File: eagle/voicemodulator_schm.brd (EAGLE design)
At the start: 80 x 83.5 mm, 27 parts, among them T1 2N5089, T2 2N5089, T3 2N5089, T4 2N5089

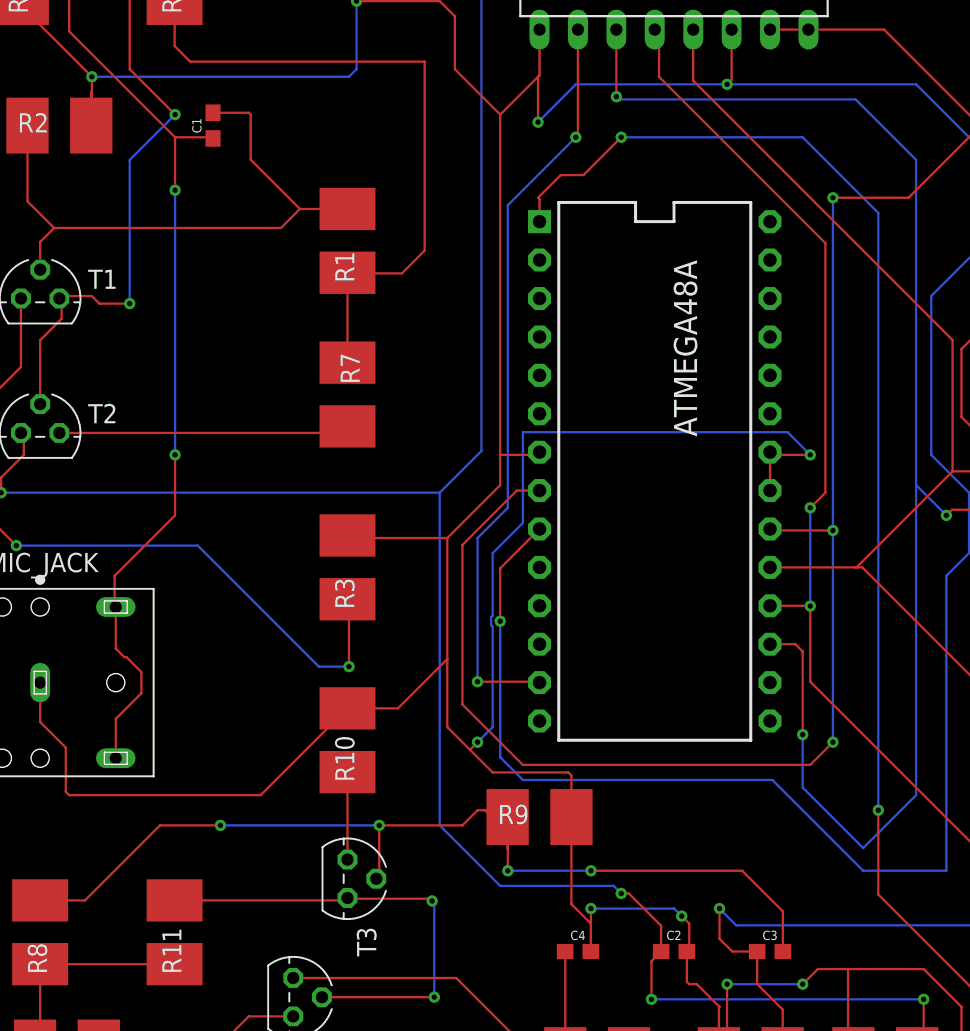
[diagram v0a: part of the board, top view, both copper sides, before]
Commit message: Pullup resistor added, testpoints at ADC in and DAC out added.
Pictures, board layout and schematic all updated.
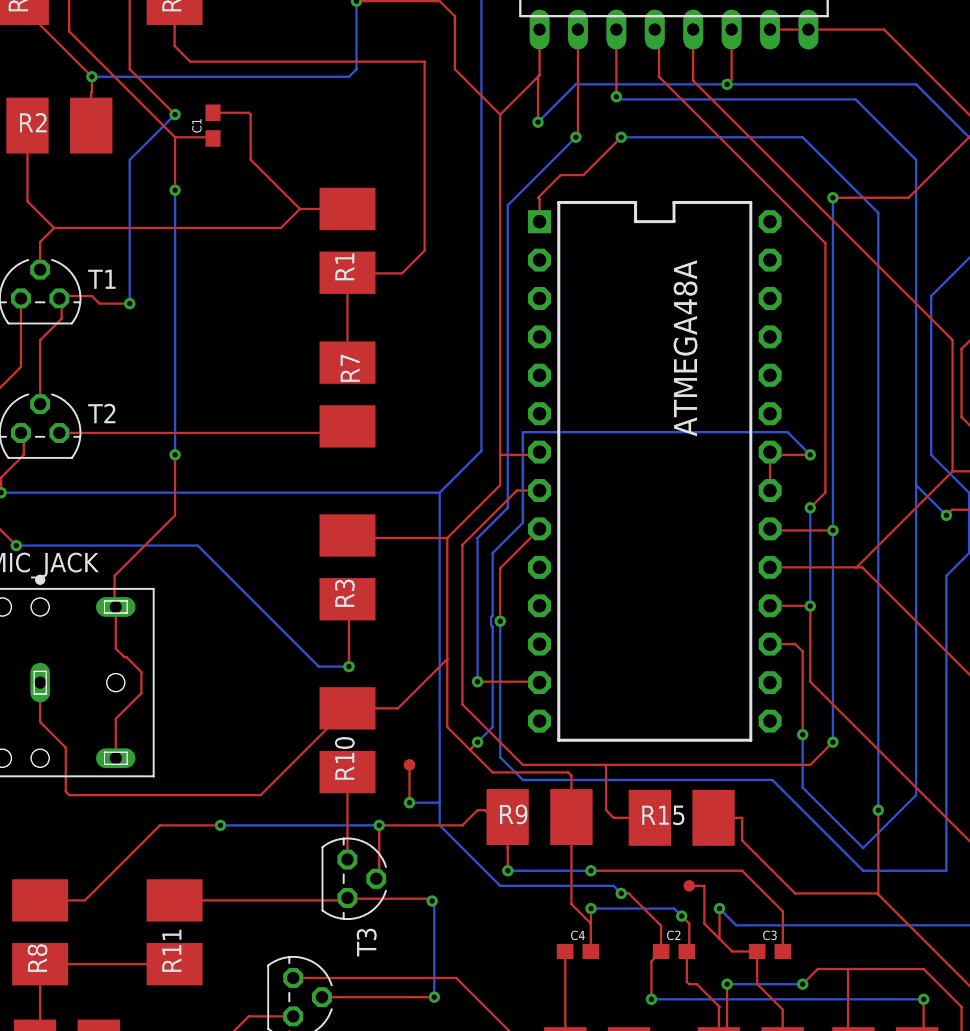
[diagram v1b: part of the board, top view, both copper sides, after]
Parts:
- added R15: (no value), resistor-shunt:SMS-WAV
- added TP1, TP2: TEST-POINT3, SparkFun-Connectors:PAD.03X.03
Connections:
- net N$22: now also R15.1
- net N$4: now also TP1.P$1
- net N$5: now also TP2.P$1
- net VCC: now also R15.2
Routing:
- net N$22: track 84.0 -> 97.9 mm
- net VCC: track 203.6 -> 209.7 mm
- net N$4: track 91.2 -> 96.2 mm
- net N$5: track 143.3 -> 147.8 mm, vias 5 -> 6
- net N$9: track 64.7 -> 62.7 mm
- net 0: track 360.4 -> 358.9 mm
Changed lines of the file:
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@@
 <attribute name="VALUE" x="20.54" y="3.965" size="1.27" layer="27" ratio="10" rot="R270"/>
+</element>
+<element name="TP1" library="SparkFun-Connectors" library_urn="urn:adsk.eagle:library:513" package="PAD.03X.03" package3d_urn="urn:adsk.eagle:package:38286/1" value="TEST-POINT3" x="48" y="14.5"/>
+<element name="TP2" library="SparkFun-Connectors" library_urn="urn:adsk.eagle:library:513" package="PAD.03X.03" package3d_urn="urn:adsk.eagle:package:38286/1" value="TEST-POINT3" x="29.5" y="22.5"/>
+<element name="R15" library="resistor-shunt" library_urn="urn:adsk.eagle:library:346" package="SMS-WAV" package3d_urn="urn:adsk.eagle:package:25223/1" value="" x="47.5" y="19">
+<attribute name="MF" value="" x="47.5" y="19" size="1.778" layer="27" display="off"/>
+<attribute name="MPN" value="" x="47.5" y="19" size="1.778" layer="27" display="off"/>
+<attribute name="NAME" x="44.7314" y="18.5428" size="1.27" layer="25"/>
+<attribute name="OC_FARNELL" value="unknown" x="47.5" y="19" size="1.778" layer="27" display="off"/>
+<attribute name="OC_NEWARK" value="unknown" x="47.5" y="19" size="1.778" layer="27" display="off"/>
+<attribute name="VALUE" x="44.452" y="16.1044" size="1.27" layer="27"/>
 </element>
 </elements>
@@
 <via x="8.5" y="68" extent="1-16" drill="0.35"/>
 <wire x1="8.5" y1="68" x2="8.5" y2="67" width="0.1524" layer="1"/>
-<wire x1="8.5" y1="67" x2="8.5" y2="65.5" width="0.1524" layer="1"/>
 <wire x1="8.5" y1="68" x2="3.81" y2="72.69" width="0.1524" layer="1"/>
 <wire x1="3.81" y1="72.69" x2="3.81" y2="72.8218" width="0.1524" layer="1"/>
@@
 <wire x1="31.5" y1="40.5" x2="2.5" y2="40.5" width="0.1524" layer="16"/>
 <via x="2.5" y="40.5" extent="1-16" drill="0.35"/>
-<wire x1="31.5" y1="40.5" x2="31.5" y2="18.5" width="0.1524" layer="16"/>
+<wire x1="31.5" y1="40.5" x2="31.5" y2="20" width="0.1524" layer="16"/>
+<wire x1="31.5" y1="20" x2="31.5" y2="18.5" width="0.1524" layer="16"/>
 <wire x1="31.5" y1="18.5" x2="35.5" y2="14.5" width="0.1524" layer="16"/>
 <wire x1="35.5" y1="14.5" x2="43" y2="14.5" width="0.1524" layer="16"/>
@@
 <wire x1="63.5" y1="7" x2="63.5" y2="3.7418" width="0.1524" layer="1"/>
 <wire x1="63.5" y1="3.7418" x2="63.0682" y2="3.31" width="0.1524" layer="1"/>
+<contactref element="TP2" pad="P$1"/>
+<wire x1="31.5" y1="20" x2="29.5" y2="20" width="0.1524" layer="16"/>
+<via x="29.5" y="20" extent="1-16" drill="0.35"/>
+<wire x1="29.5" y1="20" x2="29.5" y2="22.5" width="0.1524" layer="1"/>
 </signal>
 <signal name="N$6">
@@
 <wire x1="76" y1="51.5" x2="76.2" y2="51.3" width="0.1524" layer="1"/>
 <wire x1="76.2" y1="51.3" x2="76.2" y2="46.99" width="0.1524" layer="1"/>
+<contactref element="TP1" pad="P$1"/>
+<wire x1="50" y1="11" x2="49" y2="12" width="0.1524" layer="1"/>
+<wire x1="49" y1="12" x2="49" y2="14.5" width="0.1524" layer="1"/>
+<wire x1="49" y1="14.5" x2="48" y2="14.5" width="0.1524" layer="1"/>
 </signal>
 <signal name="N$9">
@@
 <wire x1="33" y1="18.5" x2="34" y2="19.5" width="0.1524" layer="1"/>
 <wire x1="34" y1="19.5" x2="34.5" y2="19.5" width="0.1524" layer="1"/>
-<wire x1="34.5" y1="19.5" x2="35.5418" y2="19.5" width="0.1524" layer="1"/>
 <wire x1="54.19" y1="10.16" x2="54.19" y2="12.81" width="0.1524" layer="1"/>
 <wire x1="51.5" y1="15.5" x2="54.19" y2="12.81" width="0.1524" layer="1"/>
@@
 <wire x1="36" y1="15.5" x2="36" y2="17" width="0.1524" layer="1"/>
 <via x="36" y="15.5" extent="1-16" drill="0.35"/>
-<wire x1="36" y1="17" x2="36" y2="18" width="0.1524" layer="1"/>
 <wire x1="36" y1="15.5" x2="41.5" y2="15.5" width="0.1524" layer="16"/>
 <wire x1="35.9918" y1="19.05" x2="35.9918" y2="17.0082" width="0.1524" layer="1"/>
@@
 <wire x1="33" y1="26.5" x2="37" y2="22.5" width="0.1524" layer="1"/>
 <wire x1="56" y1="22.5" x2="57.5" y2="24" width="0.1524" layer="1"/>
-<wire x1="37" y1="22.5" x2="56" y2="22.5" width="0.1524" layer="1"/>
+<wire x1="37" y1="22.5" x2="42.5" y2="22.5" width="0.1524" layer="1"/>
 <via x="57.5" y="24" extent="1-16" drill="0.35"/>
+<wire x1="42.5" y1="22.5" x2="56" y2="22.5" width="0.1524" layer="1"/>
 <wire x1="57.5" y1="24" x2="57.5" y2="38" width="0.1524" layer="16"/>
 <via x="57.5" y="38" extent="1-16" drill="0.35"/>
@@
 <via x="76" y="30.5" extent="1-16" drill="0.35"/>
 <wire x1="76" y1="30.5" x2="78" y2="30.5" width="0.1524" layer="1"/>
+<contactref element="R15" pad="2"/>
+<wire x1="45.3918" y1="19" x2="43" y2="19" width="0.1524" layer="1"/>
+<wire x1="43" y1="19" x2="42.5" y2="19.5" width="0.1524" layer="1"/>
+<wire x1="42.5" y1="19.5" x2="42.5" y2="22.5" width="0.1524" layer="1"/>
 </signal>
 <signal name="N$2">
@@
 <wire x1="38" y1="60" x2="38.1" y2="59.9" width="0.1524" layer="1"/>
 <wire x1="38.1" y1="59.9" x2="38.1" y2="58.42" width="0.1524" layer="1"/>
+<contactref element="R15" pad="1"/>
+<wire x1="60.5" y1="13.93" x2="60.43" y2="14" width="0.1524" layer="1"/>
+<wire x1="60.43" y1="14" x2="55" y2="14" width="0.1524" layer="1"/>
+<wire x1="55" y1="14" x2="51.5" y2="17.5" width="0.1524" layer="1"/>
+<wire x1="51.5" y1="17.5" x2="51.5" y2="19" width="0.1524" layer="1"/>
+<wire x1="51.5" y1="19" x2="49.6082" y2="19" width="0.1524" layer="1"/>
 </signal>
 </signals>

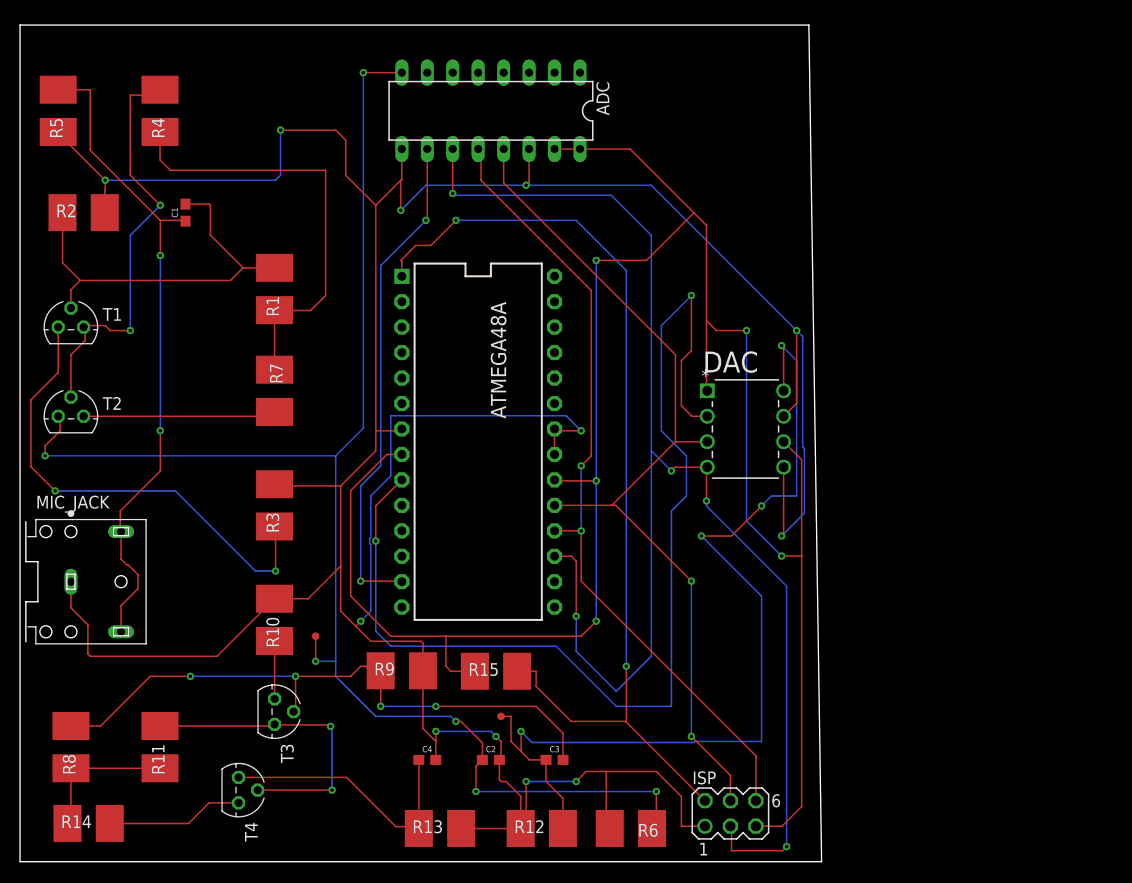
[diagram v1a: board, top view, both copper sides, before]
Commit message: Added 10 mm Power LEDs
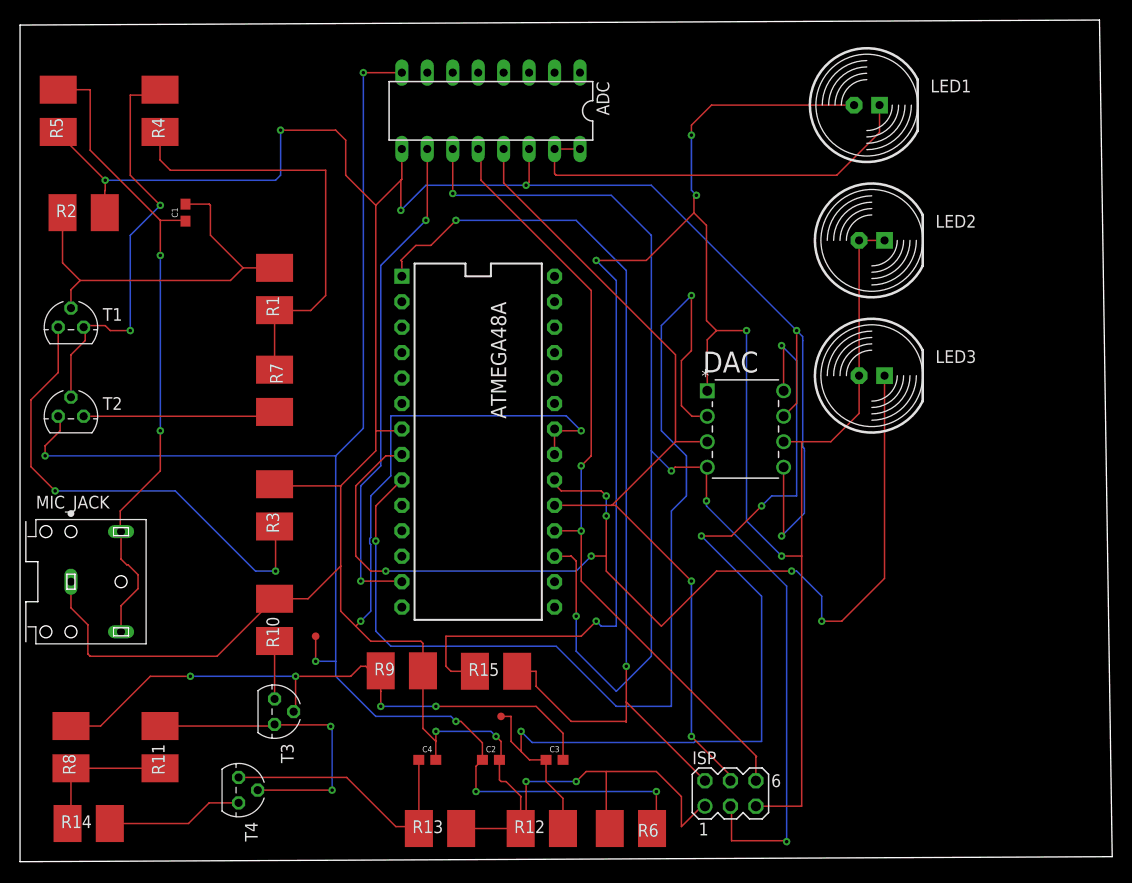
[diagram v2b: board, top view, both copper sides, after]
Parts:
- added LED1, LED2, LED3: (no value), led:LED10MM
- moved ISP 2.00 mm to (70.9, 6.81)
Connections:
- new net N$18: ADC.VDD, ADC.VREF, LED1.K
- new net N$21: ATMEGA48A.20, ATMEGA48A.8, LED3.K
- net VCC: now also LED1.A, LED2.A, LED2.K, LED3.A; no longer ADC.VDD, ADC.VREF, ATMEGA48A.20, ATMEGA48A.8
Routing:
- net N$21: track 0.00 -> 110.6 mm, vias 0 -> 6
- net N$18: track 0.00 -> 42.0 mm
- net VCC: track 209.7 -> 216.6 mm, vias 5 -> 6
- net N$2: track 80.1 -> 78.1 mm
- net N$17: track 88.8 -> 86.8 mm
- net 0: track 358.9 -> 359.8 mm
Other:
- board size 80 x 83.5 mm -> 109 x 84 mm
